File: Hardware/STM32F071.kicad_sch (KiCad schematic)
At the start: 5 parts, among them J1 USB_C_Receptacle_USB2.0_14P, U1 STM32C071K8Tx, U2 USBLC6-2P6

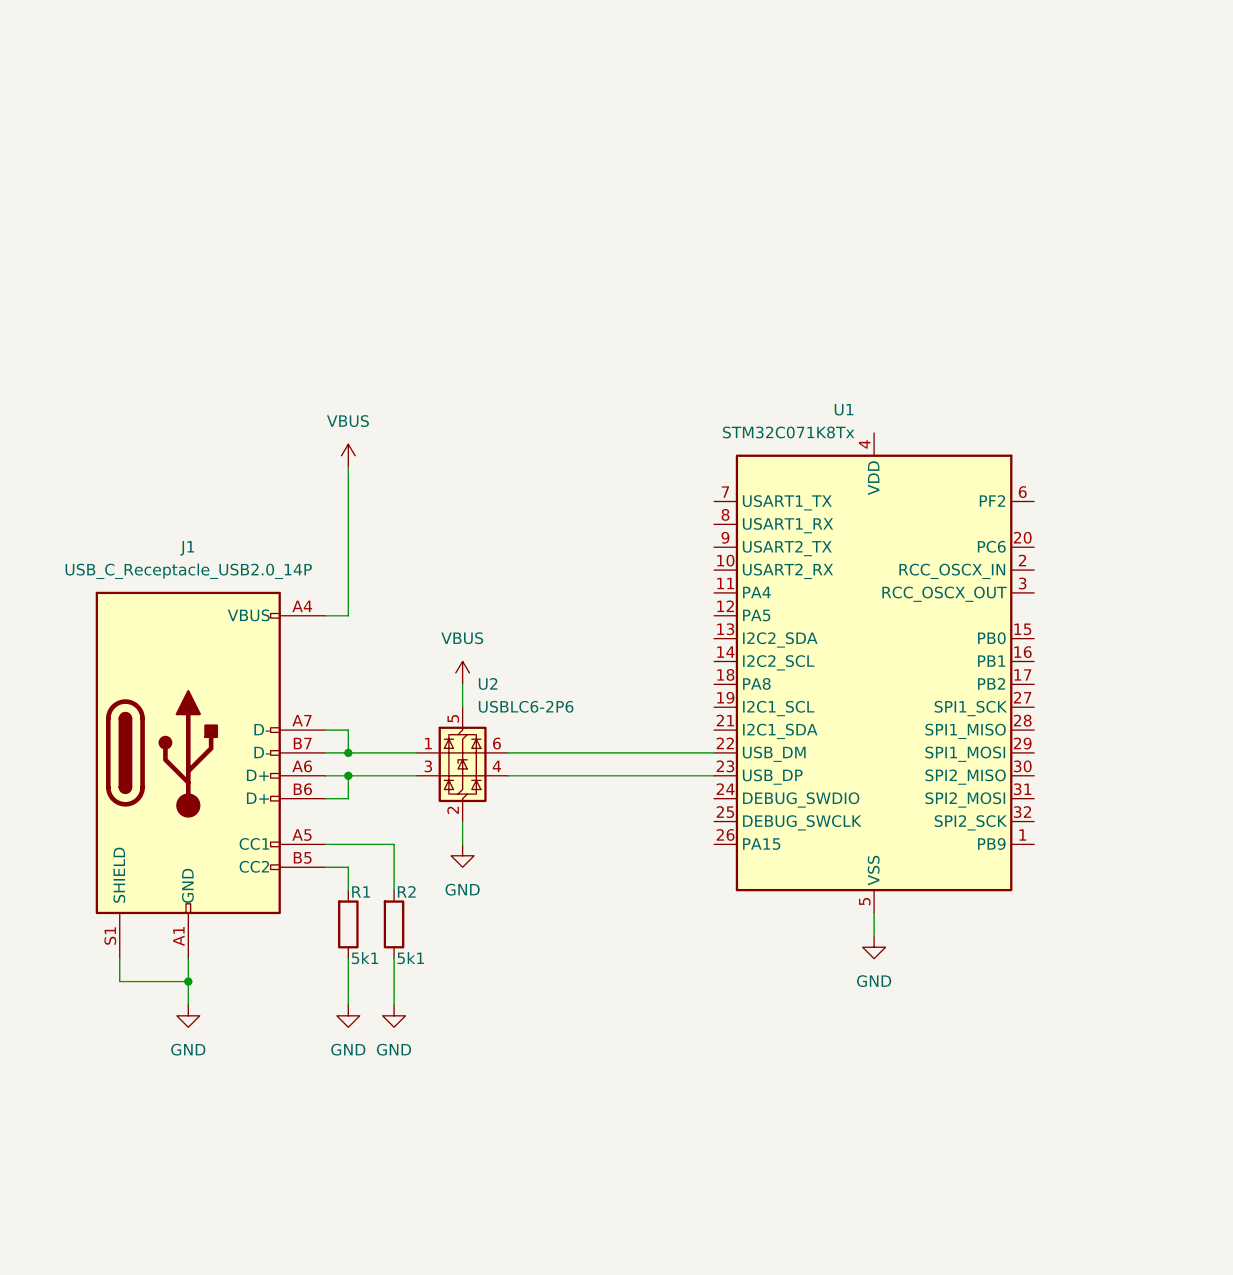
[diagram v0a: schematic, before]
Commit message: Added TPS5430 power supply. No decoupling or input caps yet
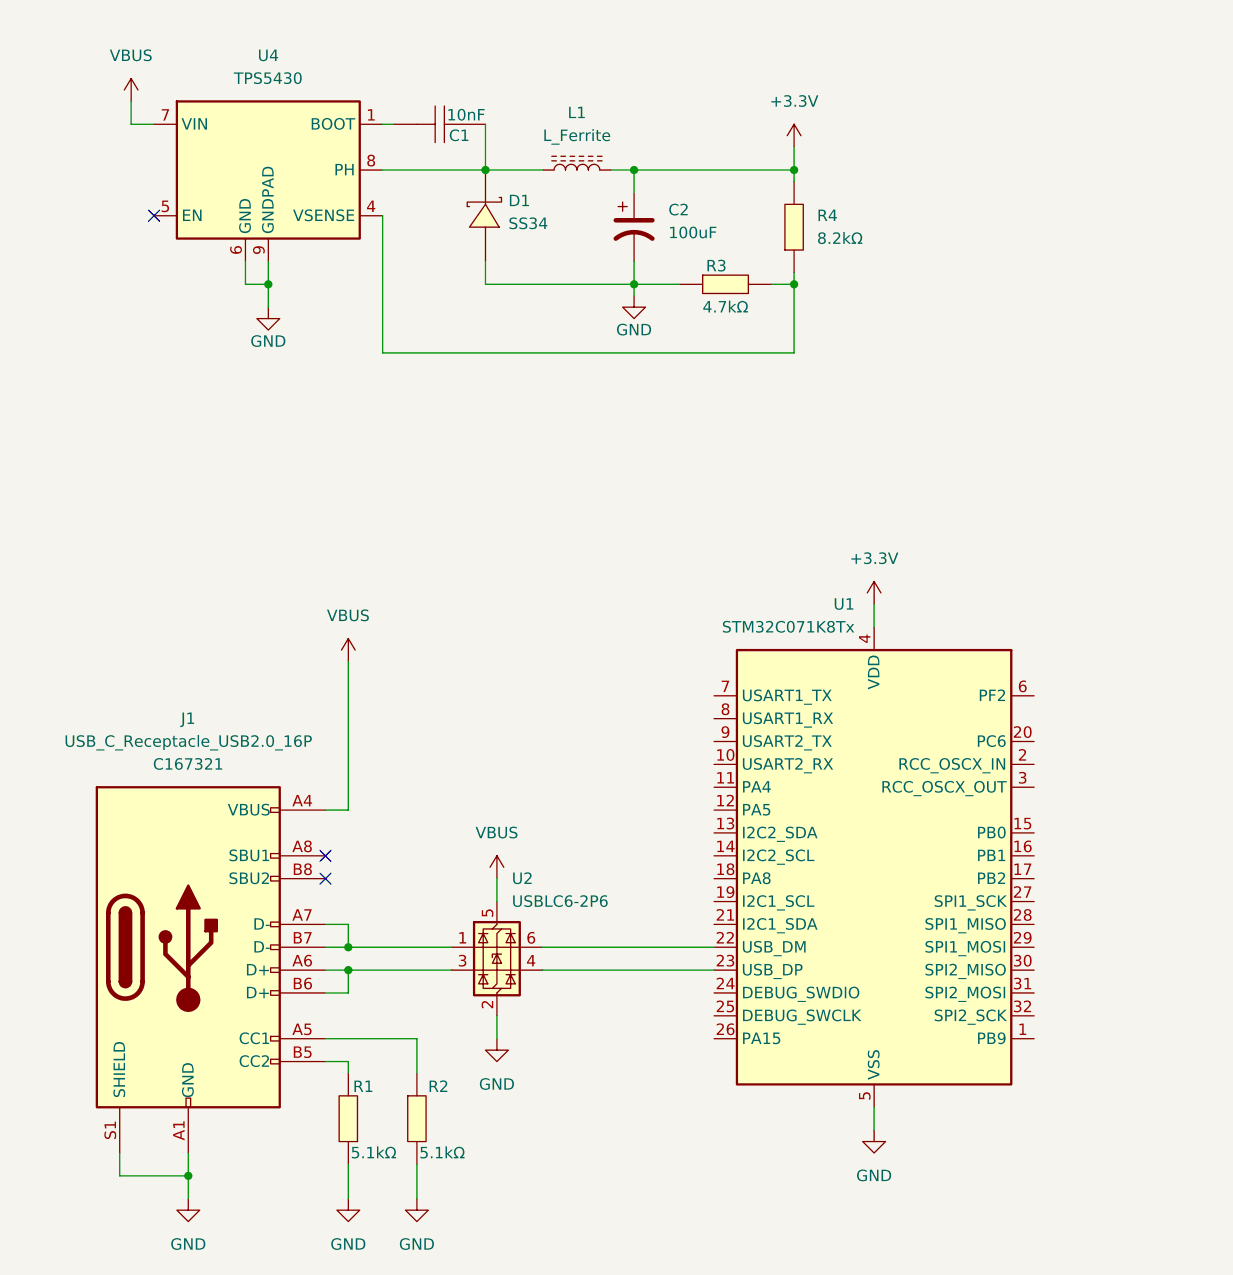
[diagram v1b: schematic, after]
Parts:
- added C1: 10nF, jlcbasic:C0805, symbol jlcbasic:10nF-0805
- added C2: 100uF, jlcbasic:CASE-B_3528, symbol jlcbasic:100uF-Tantalum
- added D1: SS34, jlcbasic:SMA_L4.3-W2.6-LS5.2-RD, symbol jlcbasic:SS34_C8678
- added L1: L_Ferrite, symbol Device:L_Ferrite
- added R3: 4.7kΩ, jlcbasic:R0805, symbol jlcbasic:4.7kΩ-0805
- added R4: 8.2kΩ, jlcbasic:R0805, symbol jlcbasic:8.2kΩ-0805
- added U4: TPS5430, Package_SO:TI_SO-PowerPAD-8_ThermalVias, symbol jlcbasic:TPS5430DDAR
- J1: value USB_C_Receptacle_USB2.0_14P -> USB_C_Receptacle_USB2.0_16P; footprint project:USB-C_SMD-TYPE-C-31-M-12 -> project:USB-C-SMD_TYPE-C-USB-17; symbol Connector:USB_C_Receptacle_USB2.0_14P -> project:USB_C_Receptacle_USB2.0_16P; LCSC Part (none) -> C167321
- R1, R2: value 5k1 -> 5.1kΩ; footprint (none) -> jlcbasic:R0805; symbol Device:R -> jlcbasic:5.1kΩ-0805; LCSC Part (none) -> C27834; PartNumber (none) -> 0805W8F5101T5E
- U2: LCSC Part (none) -> C15999
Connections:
- net GND: now also R2.2, C2.2, D1.2 (A), R3.1, U4.6 (GND), U4.9 (GNDPAD); no longer R2.1
- net VBUS: now also U4.7 (VIN)
- net +3.3V: now reaches U1.4 (VDD)
- net +3.3V: now also C2.1, L1.2, R4.2
- net at J1.A5 (CC1): now also R2.1; no longer R2.2
- new net: C1.1, D1.1 (K), L1.1, U4.8 (PH)
- new net: C1.2, U4.1 (BOOT)
- new net: R3.2, R4.1, U4.4 (VSENSE)
- no-connect marks 0 -> 3
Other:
- moved on the sheet: U1, U2

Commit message: More work on power supply
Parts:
- added C3, C4: 10uF, jlcbasic:C1206, symbol jlcbasic:10uF-1206
- added Q1: AO3401A, jlcbasic:SOT-23_L2.9-W1.3-P1.90-LS2.4-BR, symbol jlcbasic:AO3401A
- added R5: 10Ω, jlcbasic:R0805_NEW, symbol jlcbasic:10Ω-0805
- added R6: 47kΩ, jlcbasic:R0805, symbol jlcbasic:47kΩ-0805
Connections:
- net GND: now also C3.1, C4.1
- net VBUS: now also C4.2, Q1.D, R5.2
- new net: C3.2, Q1.S, R5.1, R6.2
- new net: Q1.G, R6.1
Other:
- moved on the sheet: C1, C2, D1, L1, R3, R4, U4

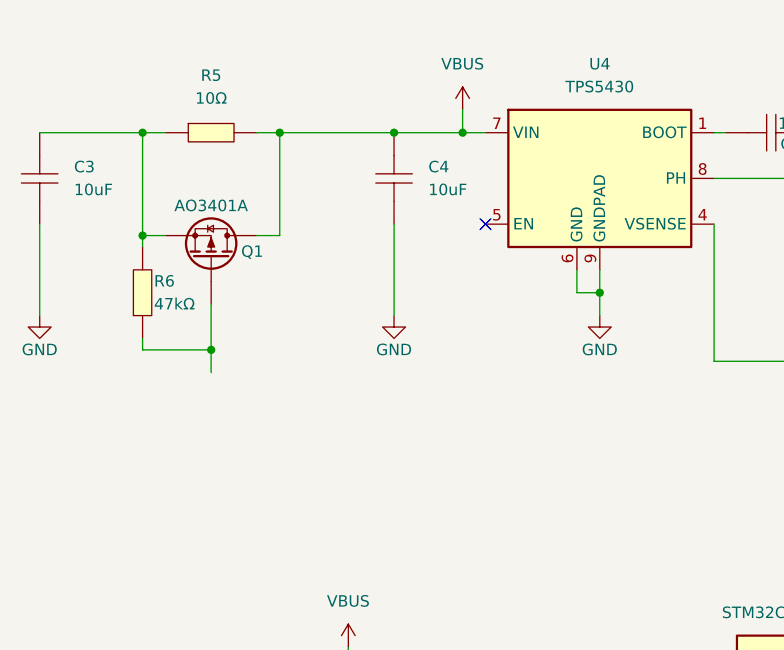
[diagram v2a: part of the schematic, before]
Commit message: Added 2n7002 to drive the power-on FET
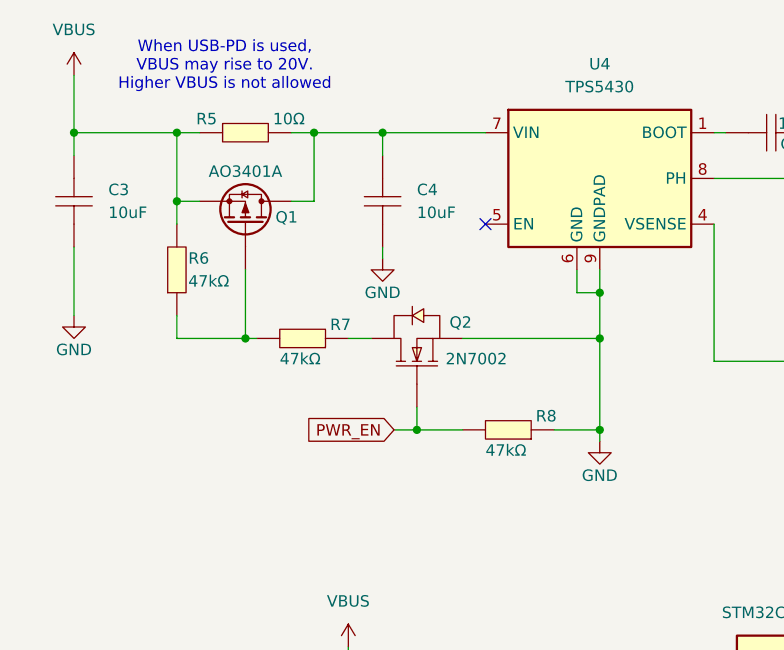
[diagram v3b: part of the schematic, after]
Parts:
- added Q2: 2N7002, jlcpreferred:SOT-23-3_L2.9-W1.3-P1.90-LS2.4-BR, symbol jlcpreferred:2N7002_C7420321
- added R7, R8: 47kΩ, jlcbasic:R0805, symbol jlcbasic:47kΩ-0805
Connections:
- net GND: now also Q2.2 (S), R8.1
- net VBUS: now also C3.2, Q1.S, R5.1, R6.2; no longer C4.2, Q1.D, R5.2, U4.7 (VIN)
- net at Q1.G, R6.1: now also R7.2
- new net: Q2.3 (D), R7.1
- new net: C4.2, Q1.D, R5.2, U4.7 (VIN)
- new net PWR_EN: Q2.1 (G), R8.2
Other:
- note added: "When USB-PD is used, VBUS may rise to 20V. Higher VBUS is not allowed"
- moved on the sheet: C3, C4, Q1, R5, R6

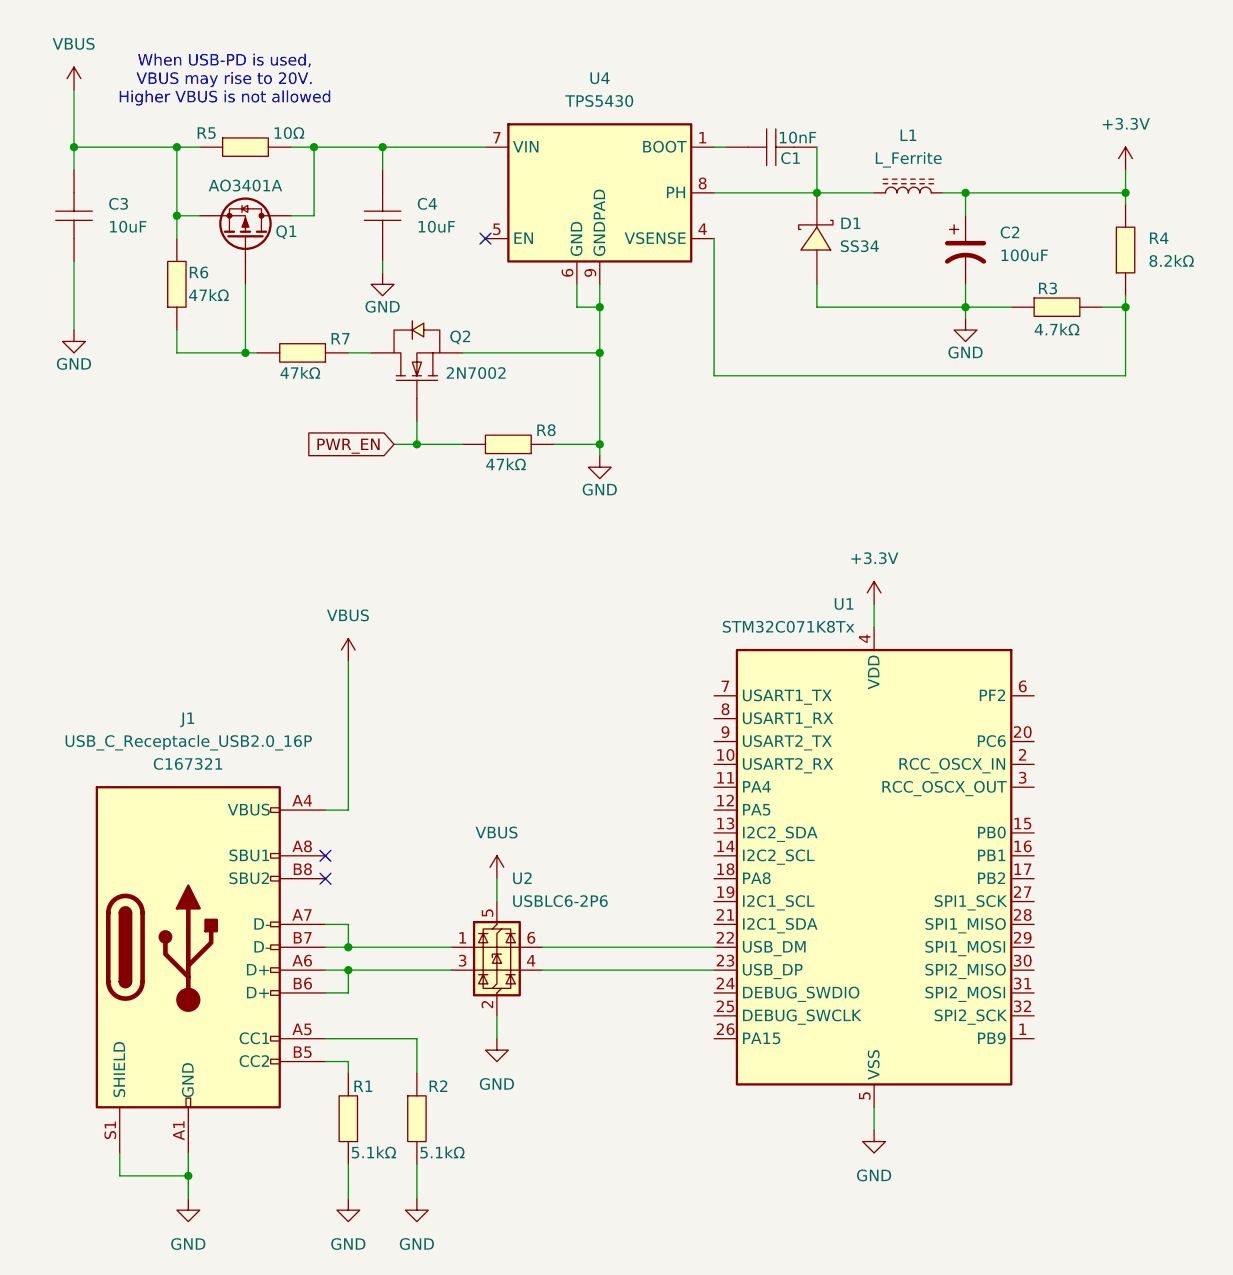
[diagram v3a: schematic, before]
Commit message: Changed power supply to XL1509. Started PCB. No inductor yet
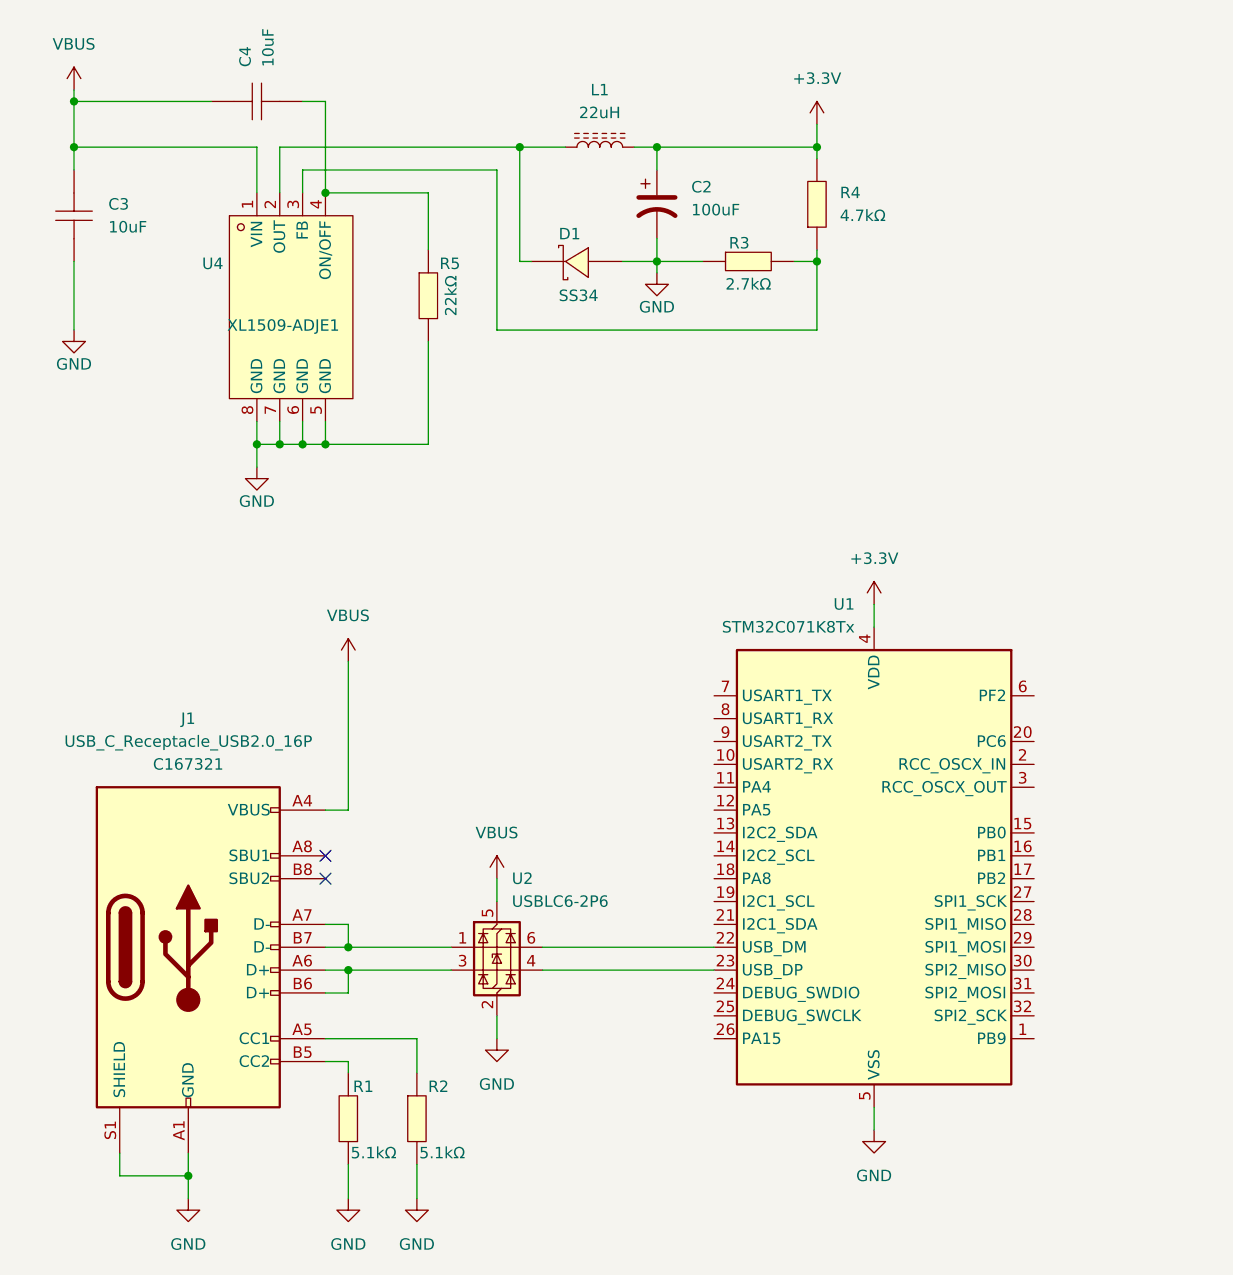
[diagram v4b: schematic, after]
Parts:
- removed C1: 10nF, jlcbasic:C0805, symbol jlcbasic:10nF-0805
- removed Q1: AO3401A, jlcbasic:SOT-23_L2.9-W1.3-P1.90-LS2.4-BR, symbol jlcbasic:AO3401A
- removed Q2: 2N7002, jlcpreferred:SOT-23-3_L2.9-W1.3-P1.90-LS2.4-BR, symbol jlcpreferred:2N7002_C7420321
- removed R5: 10Ω, jlcbasic:R0805_NEW, symbol jlcbasic:10Ω-0805
- removed R6, R7, R8: 47kΩ, jlcbasic:R0805, symbol jlcbasic:47kΩ-0805
- removed U4: TPS5430, Package_SO:TI_SO-PowerPAD-8_ThermalVias, symbol jlcbasic:TPS5430DDAR
- added R5: 22kΩ, jlcbasic:R0805, symbol jlcbasic:22kΩ-0805
- added U4: XL1509-ADJE1, jlcpreferred:SOIC-8_L5.0-W4.0-P1.27-LS6.0-BL, symbol jlcpreferred:XL1509-ADJE1
- L1: value L_Ferrite -> 22uH
- R3: value 4.7kΩ -> 2.7kΩ; symbol jlcbasic:4.7kΩ-0805 -> jlcbasic:2.7kΩ-0805; LCSC Part C17673 -> C17530; PartNumber 0805W8F4701T5E -> 0805W8F2701T5E
- R4: value 8.2kΩ -> 4.7kΩ; symbol jlcbasic:8.2kΩ-0805 -> jlcbasic:4.7kΩ-0805; LCSC Part C17828 -> C17673; PartNumber 0805W8F8201T5E -> 0805W8F4701T5E
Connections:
- net GND: now also R5.2, U4.5 (GND), U4.6 (GND), U4.7 (GND), U4.8 (GND); no longer C4.1
- net VBUS: now also C4.2, U4.1 (VIN)
- net at D1.1 (K), L1.1: now also U4.2 (OUT)
- net at R3.2, R4.1: now also U4.3 (FB)
- new net: C4.1, R5.1, U4.4 (ON/OFF)
- no-connect marks 3 -> 2
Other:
- note removed: "When USB-PD is used, VBUS may rise to 20V. Higher VBUS is not allowed"
- moved on the sheet: C2, D1, L1, R3, R4

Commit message: New Power supply and USB connector laid out
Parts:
- added C5: 10uF, jlcbasic:C1206, symbol jlcbasic:10uF-1206
- L1: value 22uH -> 100uH; footprint (none) -> project:IND-SMD_L4.0-W4.0_SMNR4030; LCSC Part (none) -> C135278; PartNumber (none) -> SMNR4030-101MT
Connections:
- net +3.3V: now also C5.2
- net GND: now also C5.1
- net at U1.22 (PA11): now also U2.3 (I/O2); no longer U2.6 (I/O1)
- net at U1.23 (PA12): now also U2.1 (I/O1); no longer U2.4 (I/O2)
- net at J1.A6 (D+), J1.B6 (D+): now also U2.6 (I/O1); no longer U2.3 (I/O2)
- net at J1.A7 (D-), J1.B7 (D-): now also U2.4 (I/O2); no longer U2.1 (I/O1)
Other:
- moved on the sheet: C2, R3, R4
